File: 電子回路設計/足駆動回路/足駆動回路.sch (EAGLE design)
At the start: 22 parts, among them CN1 798-HVH-280-3P-6.5DS, IC1 TC74HC244AF, U1 BTN9990LV, U2 BTN9990LV

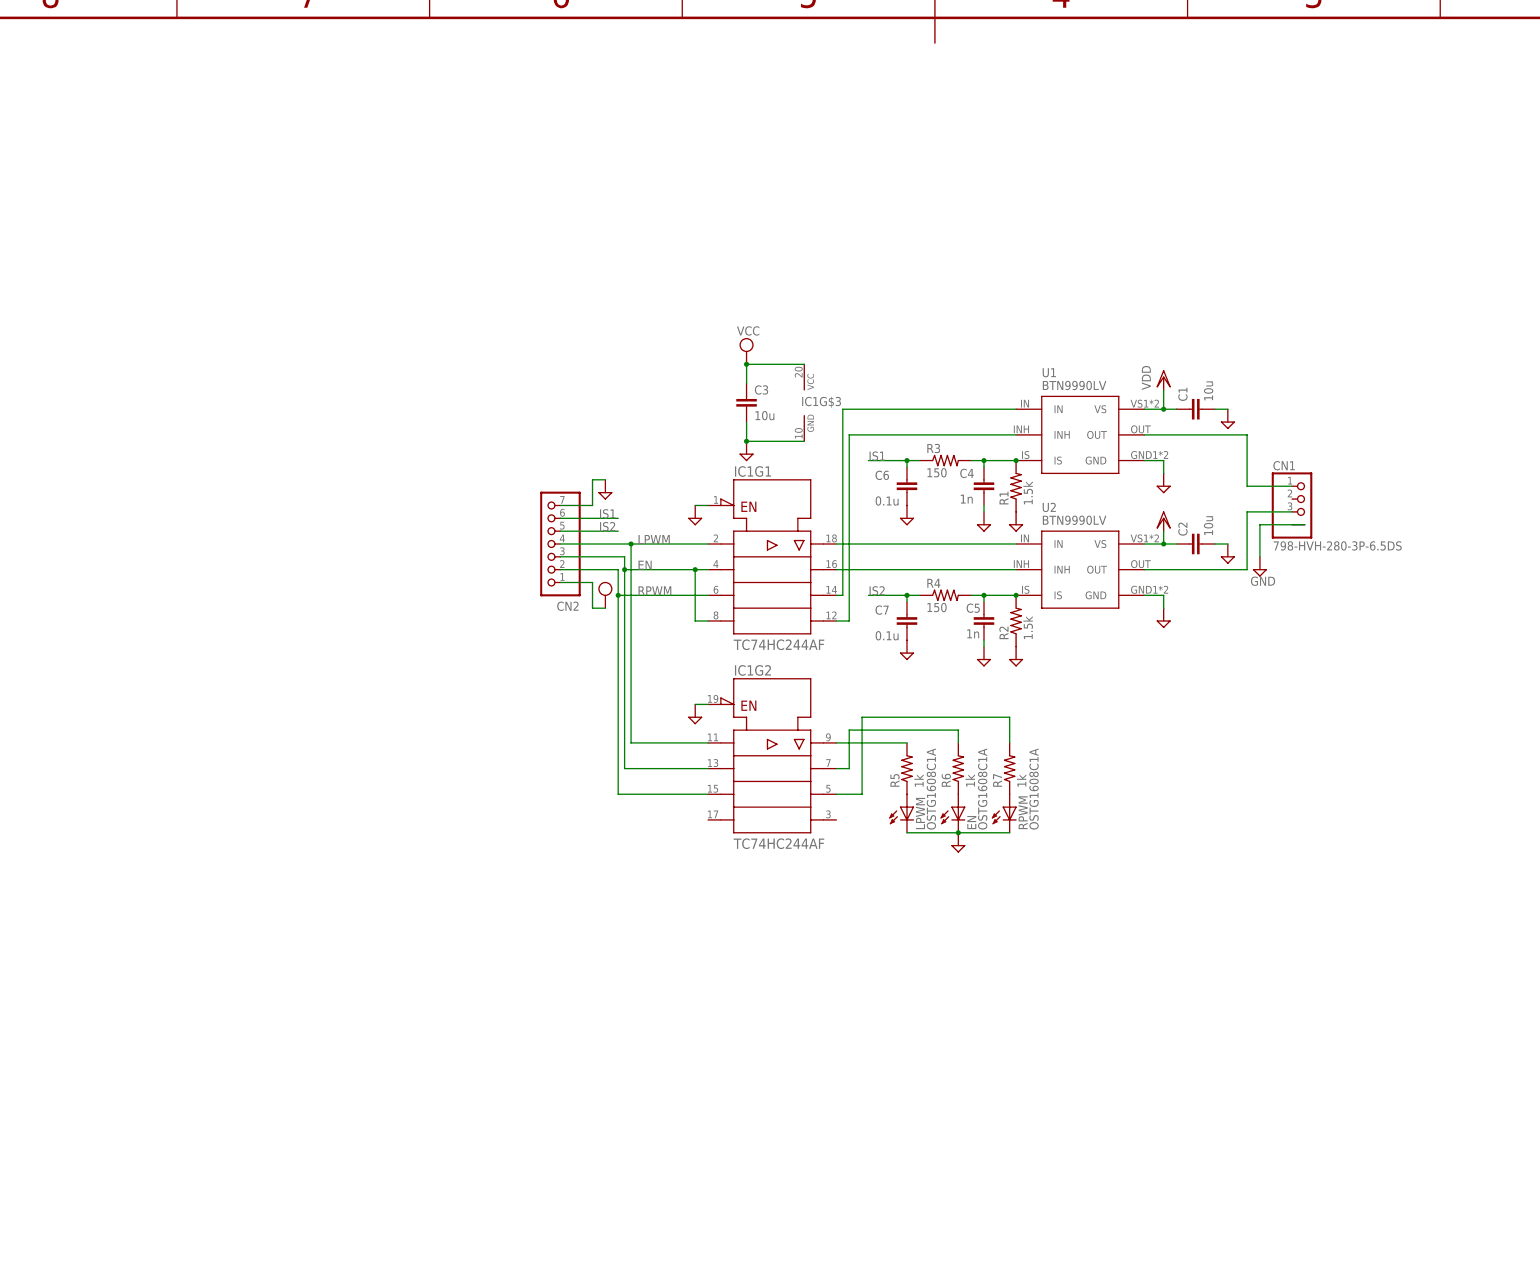
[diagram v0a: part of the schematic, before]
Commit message: ・足駆動回路設計完 ・足駆動回路ミラーバージョン作成
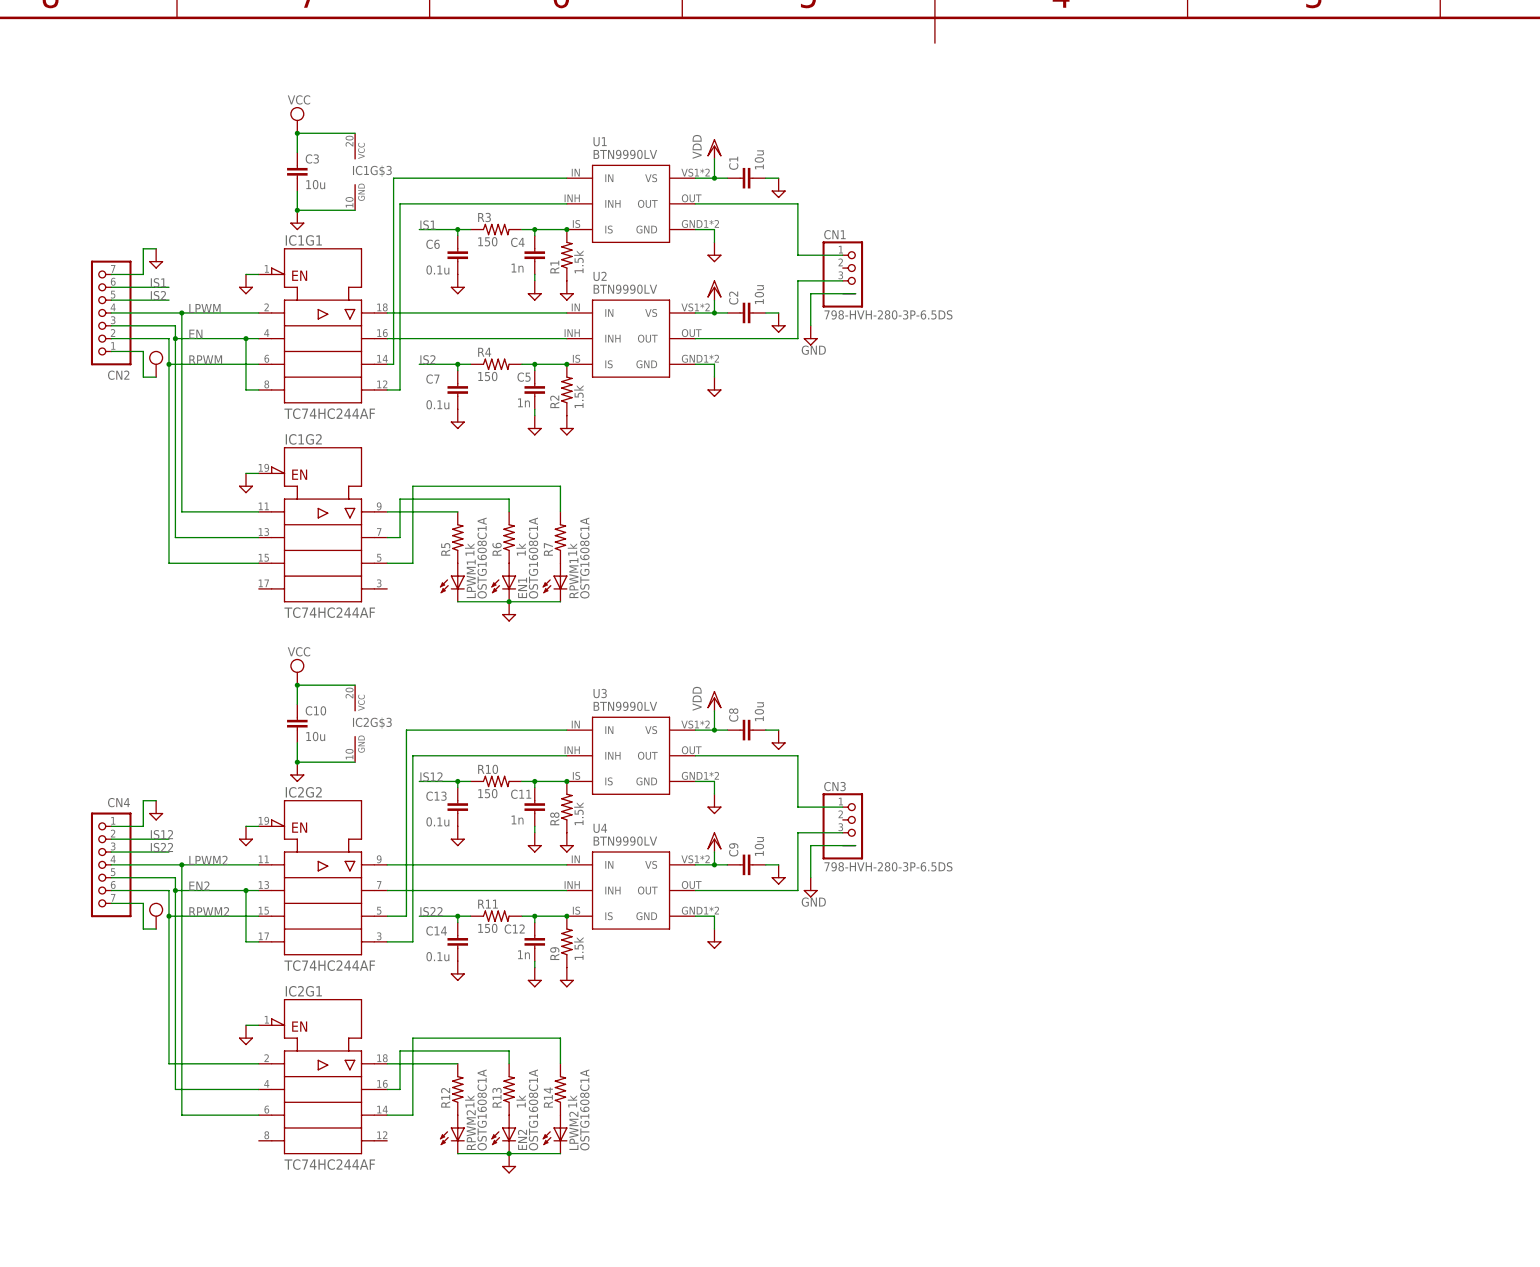
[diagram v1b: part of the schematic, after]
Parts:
- removed EN, LPWM, RPWM: OSTG1608C1A, LED:OSTG1608C1A
- added C10, C8, C9: 10u, RCL:C2012
- added C11, C12: 1n, RCL:C1608
- added C13, C14: 0.1u, RCL:C1608
- added CN3: 798-HVH-280-3P-6.5DS, HVH-280:798-HVH-280-3P-6.5DS
- added CN4: (no value), jst-xh:B7B-XH-A
- added EN1, EN2, LPWM1, LPWM2, RPWM1, RPWM2: OSTG1608C1A, LED:OSTG1608C1A
- added IC2: TC74HC244AF, 東芝_74LSシリーズ:TC74HC244AF
- added R10, R11: 150, RCL:R1608
- added R12, R13, R14: 1k, RCL:R1608
- added R8, R9: 1.5k, RCL:R1608
- added U3, U4: BTN9990LV, IT_MotorControlIC:BTN9990LV
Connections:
- new net EN2: CN4.5, IC2G1.A2, IC2G2.A2, IC2G2.A4
- new net IS12: C13.1, CN4.2, R10.1
- new net IS1_A1: C11.1, R10.2, R8.2, U3.IS
- new net IS22: C14.1, CN4.3, R11.1
- new net IS2_2: C12.1, R11.2, R9.2, U4.IS
- new net LPWM2: CN4.4, IC2G1.A3, IC2G2.A1
- new net N$11: IC2G2.Y1, U4.IN
- new net N$12: IC2G2.Y2, U4.INH
- new net N$13: IC2G2.Y3, U3.IN
- new net N$14: IC2G2.Y4, U3.INH
- new net N$15: R12.1, RPWM2.A
- new net N$16: EN2.A, R13.1
- new net N$17: LPWM2.A, R14.1
- new net N$18: IC2G1.Y1, R12.2
- new net N$19: IC2G1.Y2, R13.2
- new net N$20: IC2G1.Y3, R14.2
- new net OUT3: CN3.1, U3.OUT
- new net OUT4: CN3.3, U4.OUT
- new net RPWM2: CN4.6, IC2G1.A1, IC2G2.A3
- net GND: now also C10.2, C11.2, C12.2, C13.2, C14.2, C8.2, C9.2, CN3.P$1, CN4.1, EN1.C, EN2.C, IC2G$3.GND, IC2G1.!G, IC2G2.!G, LPWM1.C, LPWM2.C, R8.1, R9.1, RPWM1.C, RPWM2.C, U3.GND, U4.GND; no longer EN.C, LPWM.C, RPWM.C
- net N$5: now also LPWM1.A; no longer LPWM.A
- net N$6: now also EN1.A; no longer EN.A
- net N$7: now also RPWM1.A; no longer RPWM.A
- net VCC: now also C10.1, CN4.7, IC2G$3.VCC
- net VDD: now also C8.1, C9.1, U3.VS, U4.VS
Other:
- moved on the sheet: C1, C2, C3, C4, C5, C6, C7, CN1, CN2, IC1G$3, IC1G1, IC1G2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

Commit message: fix : RMD cap
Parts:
- C1, C10, C2, C3, C8, C9: device RCL:C2012 -> 村田製作所_チップセラミックコンデンサ:GCM31CD71H106KE36K
- C11, C12, C4, C5: device RCL:C1608 -> 村田製作所_チップセラミックコンデンサ:GCM188R91H102KA37D
- C13, C14, C6, C7: device RCL:C1608 -> 村田製作所_チップセラミックコンデンサ:GCM188L81H104KA57D
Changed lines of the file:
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@@
 <setting verticaltext="up"/>
 </settings>
-<grid distance="0.05" unitdist="inch" unit="inch" style="lines" multiple="1" display="yes" altdistance="0.01" altunitdist="inch" altunit="inch"/>
+<grid distance="0.1" unitdist="inch" unit="inch" style="lines" multiple="1" display="yes" altdistance="0.01" altunitdist="inch" altunit="inch"/>
 <layers>
 <layer number="1" name="Top" color="4" fill="1" visible="no" active="no"/>
@@
 <part name="SUPPLY1" library="supply2" library_urn="urn:adsk.eagle:library:372" deviceset="GND" device=""/>
 <part name="SUPPLY2" library="supply2" library_urn="urn:adsk.eagle:library:372" deviceset="GND" device=""/>
-<part name="C1" library="RCL" deviceset="C" device="2012" package3d_urn="urn:adsk.eagle:package:23617/2" value="10u"/>
-<part name="C2" library="RCL" deviceset="C" device="2012" package3d_urn="urn:adsk.eagle:package:23617/2" value="10u"/>
+<part name="C1" library="村田製作所_チップセラミックコンデンサ" deviceset="GCM?*" device="31" package3d_urn="urn:adsk.eagle:package:38657526/2" technology="CD71H106KE36K" value="10u"/>
+<part name="C2" library="村田製作所_チップセラミックコンデンサ" deviceset="GCM?*" device="31" package3d_urn="urn:adsk.eagle:package:38657526/2" technology="CD71H106KE36K" value="10u"/>
 <part name="VDD2" library="supply1" library_urn="urn:adsk.eagle:library:371" deviceset="VDD" device=""/>
 <part name="SUPPLY3" library="supply2" library_urn="urn:adsk.eagle:library:372" deviceset="GND" device=""/>
@@
 <part name="SUPPLY6" library="supply2" library_urn="urn:adsk.eagle:library:372" deviceset="VCC" device=""/>
 <part name="SUPPLY7" library="supply2" library_urn="urn:adsk.eagle:library:372" deviceset="GND" device=""/>
-<part name="C3" library="RCL" deviceset="C" device="2012" package3d_urn="urn:adsk.eagle:package:23617/2" value="10u"/>
+<part name="C3" library="村田製作所_チップセラミックコンデンサ" deviceset="GCM?*" device="31" package3d_urn="urn:adsk.eagle:package:38657526/2" technology="CD71H106KE36K" value="10u"/>
 <part name="SUPPLY8" library="supply2" library_urn="urn:adsk.eagle:library:372" deviceset="GND" device=""/>
 <part name="SUPPLY9" library="supply2" library_urn="urn:adsk.eagle:library:372" deviceset="GND" device=""/>
@@
 <part name="SUPPLY10" library="supply2" library_urn="urn:adsk.eagle:library:372" deviceset="GND" device=""/>
 <part name="SUPPLY11" library="supply2" library_urn="urn:adsk.eagle:library:372" deviceset="GND" device=""/>
-<part name="C4" library="RCL" deviceset="C" device="1608" package3d_urn="urn:adsk.eagle:package:23616/2" value="1n"/>
-<part name="C5" library="RCL" deviceset="C" device="1608" package3d_urn="urn:adsk.eagle:package:23616/2" value="1n"/>
+<part name="C4" library="村田製作所_チップセラミックコンデンサ" deviceset="GCM?*" device="188" package3d_urn="urn:adsk.eagle:package:38236525/2" technology="R91H102KA37D" value="1n"/>
+<part name="C5" library="村田製作所_チップセラミックコンデンサ" deviceset="GCM?*" device="188" package3d_urn="urn:adsk.eagle:package:38236525/2" technology="R91H102KA37D" value="1n"/>
 <part name="SUPPLY12" library="supply2" library_urn="urn:adsk.eagle:library:372" deviceset="GND" device=""/>
 <part name="SUPPLY13" library="supply2" library_urn="urn:adsk.eagle:library:372" deviceset="GND" device=""/>
 <part name="R3" library="RCL" deviceset="R" device="1608" package3d_urn="urn:adsk.eagle:package:23555/3" value="150"/>
-<part name="C6" library="RCL" deviceset="C" device="1608" package3d_urn="urn:adsk.eagle:package:23616/2" value="0.1u"/>
+<part name="C6" library="村田製作所_チップセラミックコンデンサ" deviceset="GCM?*" device="188" package3d_urn="urn:adsk.eagle:package:38236525/2" technology="L81H104KA57D" value="0.1u"/>
 <part name="R4" library="RCL" deviceset="R" device="1608" package3d_urn="urn:adsk.eagle:package:23555/3" value="150"/>
-<part name="C7" library="RCL" deviceset="C" device="1608" package3d_urn="urn:adsk.eagle:package:23616/2" value="0.1u"/>
+<part name="C7" library="村田製作所_チップセラミックコンデンサ" deviceset="GCM?*" device="188" package3d_urn="urn:adsk.eagle:package:38236525/2" technology="L81H104KA57D" value="0.1u"/>
 <part name="SUPPLY14" library="supply2" library_urn="urn:adsk.eagle:library:372" deviceset="GND" device=""/>
 <part name="SUPPLY15" library="supply2" library_urn="urn:adsk.eagle:library:372" deviceset="GND" device=""/>
@@
 <part name="SUPPLY19" library="supply2" library_urn="urn:adsk.eagle:library:372" deviceset="GND" device=""/>
 <part name="SUPPLY20" library="supply2" library_urn="urn:adsk.eagle:library:372" deviceset="GND" device=""/>
-<part name="C8" library="RCL" deviceset="C" device="2012" package3d_urn="urn:adsk.eagle:package:23617/2" value="10u"/>
-<part name="C9" library="RCL" deviceset="C" device="2012" package3d_urn="urn:adsk.eagle:package:23617/2" value="10u"/>
+<part name="C8" library="村田製作所_チップセラミックコンデンサ" deviceset="GCM?*" device="31" package3d_urn="urn:adsk.eagle:package:38657526/2" technology="CD71H106KE36K" value="10u"/>
+<part name="C9" library="村田製作所_チップセラミックコンデンサ" deviceset="GCM?*" device="31" package3d_urn="urn:adsk.eagle:package:38657526/2" technology="CD71H106KE36K" value="10u"/>
 <part name="VDD4" library="supply1" library_urn="urn:adsk.eagle:library:371" deviceset="VDD" device=""/>
 <part name="SUPPLY21" library="supply2" library_urn="urn:adsk.eagle:library:372" deviceset="GND" device=""/>
@@
 <part name="SUPPLY24" library="supply2" library_urn="urn:adsk.eagle:library:372" deviceset="VCC" device=""/>
 <part name="SUPPLY25" library="supply2" library_urn="urn:adsk.eagle:library:372" deviceset="GND" device=""/>
-<part name="C10" library="RCL" deviceset="C" device="2012" package3d_urn="urn:adsk.eagle:package:23617/2" value="10u"/>
+<part name="C10" library="村田製作所_チップセラミックコンデンサ" deviceset="GCM?*" device="31" package3d_urn="urn:adsk.eagle:package:38657526/2" technology="CD71H106KE36K" value="10u"/>
 <part name="SUPPLY26" library="supply2" library_urn="urn:adsk.eagle:library:372" deviceset="GND" device=""/>
 <part name="SUPPLY27" library="supply2" library_urn="urn:adsk.eagle:library:372" deviceset="GND" device=""/>
@@
 <part name="SUPPLY28" library="supply2" library_urn="urn:adsk.eagle:library:372" deviceset="GND" device=""/>
 <part name="SUPPLY29" library="supply2" library_urn="urn:adsk.eagle:library:372" deviceset="GND" device=""/>
-<part name="C11" library="RCL" deviceset="C" device="1608" package3d_urn="urn:adsk.eagle:package:23616/2" value="1n"/>
-<part name="C12" library="RCL" deviceset="C" device="1608" package3d_urn="urn:adsk.eagle:package:23616/2" value="1n"/>
+<part name="C11" library="村田製作所_チップセラミックコンデンサ" deviceset="GCM?*" device="188" package3d_urn="urn:adsk.eagle:package:38236525/2" technology="R91H102KA37D" value="1n"/>
+<part name="C12" library="村田製作所_チップセラミックコンデンサ" deviceset="GCM?*" device="188" package3d_urn="urn:adsk.eagle:package:38236525/2" technology="R91H102KA37D" value="1n"/>
 <part name="SUPPLY30" library="supply2" library_urn="urn:adsk.eagle:library:372" deviceset="GND" device=""/>
 <part name="SUPPLY31" library="supply2" library_urn="urn:adsk.eagle:library:372" deviceset="GND" device=""/>
 <part name="R10" library="RCL" deviceset="R" device="1608" package3d_urn="urn:adsk.eagle:package:23555/3" value="150"/>
-<part name="C13" library="RCL" deviceset="C" device="1608" package3d_urn="urn:adsk.eagle:package:23616/2" value="0.1u"/>
+<part name="C13" library="村田製作所_チップセラミックコンデンサ" deviceset="GCM?*" device="188" package3d_urn="urn:adsk.eagle:package:38236525/2" technology="L81H104KA57D" value="0.1u"/>
 <part name="R11" library="RCL" deviceset="R" device="1608" package3d_urn="urn:adsk.eagle:package:23555/3" value="150"/>
-<part name="C14" library="RCL" deviceset="C" device="1608" package3d_urn="urn:adsk.eagle:package:23616/2" value="0.1u"/>
+<part name="C14" library="村田製作所_チップセラミックコンデンサ" deviceset="GCM?*" device="188" package3d_urn="urn:adsk.eagle:package:38236525/2" technology="L81H104KA57D" value="0.1u"/>
 <part name="SUPPLY32" library="supply2" library_urn="urn:adsk.eagle:library:372" deviceset="GND" device=""/>
 <part name="SUPPLY33" library="supply2" library_urn="urn:adsk.eagle:library:372" deviceset="GND" device=""/>
